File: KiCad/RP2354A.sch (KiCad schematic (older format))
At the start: 18 parts, among them J11 Conn_01x02, J16 USB_C_Receptacle_USB2.0, U16 RP2354A, Y1 ABM8-272-T3

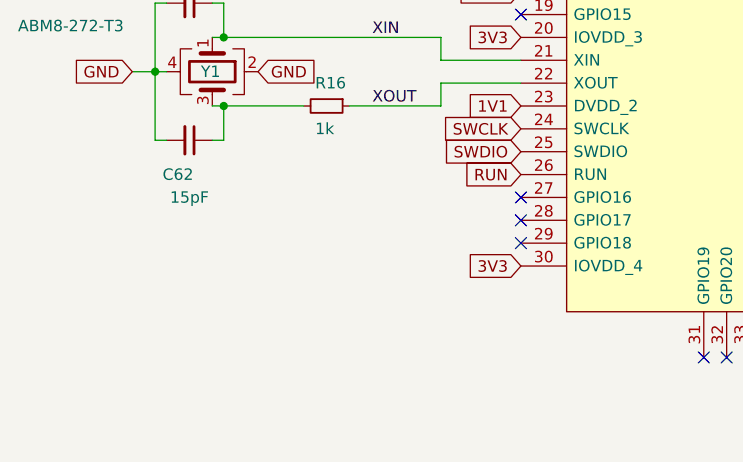
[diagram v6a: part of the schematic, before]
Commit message: Add push-button BT2 as a RESET-button on the RUN-signal
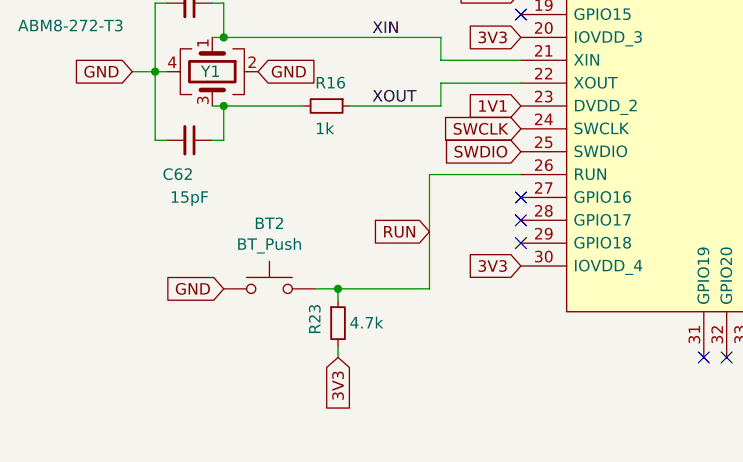
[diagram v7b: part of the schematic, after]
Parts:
- added BT2: BT_Push, SF2000:Sunrom_Tactile_Switch_3x4x2mm_SMD_2-Pin, symbol Switch:SW_Push
- added R23: 4.7k, Resistor_SMD:R_0603_1608Metric_Pad0.98x0.95mm_HandSolder, symbol Device:R_Small
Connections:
- net 3V3: now also R23.2
- net GND: now also BT2.1
- net RUN: now also BT2.2, R23.1
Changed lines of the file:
@@
 Text GLabel 3700 3600 0    50   Input ~ 0
 SWDIO
-Text GLabel 3700 3700 0    50   Input ~ 0
+Text GLabel 3300 3950 0    50   Input ~ 0
 RUN
 Text GLabel 6900 4100 2    50   Input ~ 0
@@
 Text Label 7300 4000 0    50   ~ 0
 VREG_LX
+$Comp
+L Switch:SW_Push BT2
+U 1 1 6B0575C8
+P 2600 4200
+F 0 "BT2" H 2600 4485 50  0000 C CNN
+F 1 "BT_Push" H 2600 4394 50  0000 C CNN
+F 2 "SF2000:Sunrom_Tactile_Switch_3x4x2mm_SMD_2-Pin" H 2600 4400 50  0001 C CNN
+F 3 "~" H 2600 4400 50  0001 C CNN
+	1    2600 4200
+	1    0    0    -1
+$EndComp
+Wire Wire Line
+	3700 3700 3300 3700
+Text GLabel 2400 4200 0    50   Input ~ 0
+GND
+$Comp
+L Device:R_Small R?
+U 1 1 6B05EE3D
+P 2900 4350
+AR Path="/6B05EE3D" Ref="R?"  Part="1"
+AR Path="/6AFE5B10/6B05EE3D" Ref="R23"  Part="1"
+F 0 "R23" V 2800 4300 50  0000 L CNN
+F 1 "4.7k" H 2950 4350 50  0000 L CNN
+F 2 "Resistor_SMD:R_0603_1608Metric_Pad0.98x0.95mm_HandSolder" H 2900 4350 50  0001 C CNN
+F 3 "~" H 2900 4350 50  0001 C CNN
+	1    2900 4350
+	1    0    0    -1
+$EndComp
+Wire Wire Line
+	3300 3700 3300 4200
+Text GLabel 2900 4500 3    50   Input ~ 0
+3V3
+Wire Wire Line
+	2800 4200 2900 4200
+Wire Wire Line
+	2900 4250 2900 4200
+Connection ~ 2900 4200
+Wire Wire Line
+	2900 4200 3300 4200
+Wire Wire Line
+	2900 4450 2900 4500
 $EndSCHEMATC

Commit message: Move C40 cap to RP2354A and the RESET-button circuit, change to 100nF value
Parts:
- added C40: 0.1uF, Capacitor_SMD:C_0603_1608Metric_Pad1.08x0.95mm_HandSolder, symbol Device:C
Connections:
- net GND: now also C40.2
- net RUN: now also C40.1
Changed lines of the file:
@@
 Wire Wire Line
 	2900 4450 2900 4500
+$Comp
+L Device:C C40
+U 1 1 6B09868D
+P 3300 4350
+F 0 "C40" H 3350 4450 50  0000 L CNN
+F 1 "0.1uF" H 3350 4250 50  0000 L CNN
+F 2 "Capacitor_SMD:C_0603_1608Metric_Pad1.08x0.95mm_HandSolder" H 3338 4200 50  0001 C CNN
+F 3 "~" H 3300 4350 50  0001 C CNN
+	1    3300 4350
+	1    0    0    -1
+$EndComp
+Connection ~ 3300 4200
+Text GLabel 3300 4500 3    50   Input ~ 0
+GND
 $EndSCHEMATC
